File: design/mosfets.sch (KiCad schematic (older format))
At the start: 15 parts, among them Q10 IRFS3006, Q11 IRFS3006, Q12 IRFS3006, Q7 IRFS3006, Q8 IRFS3006, Q9 IRFS3006

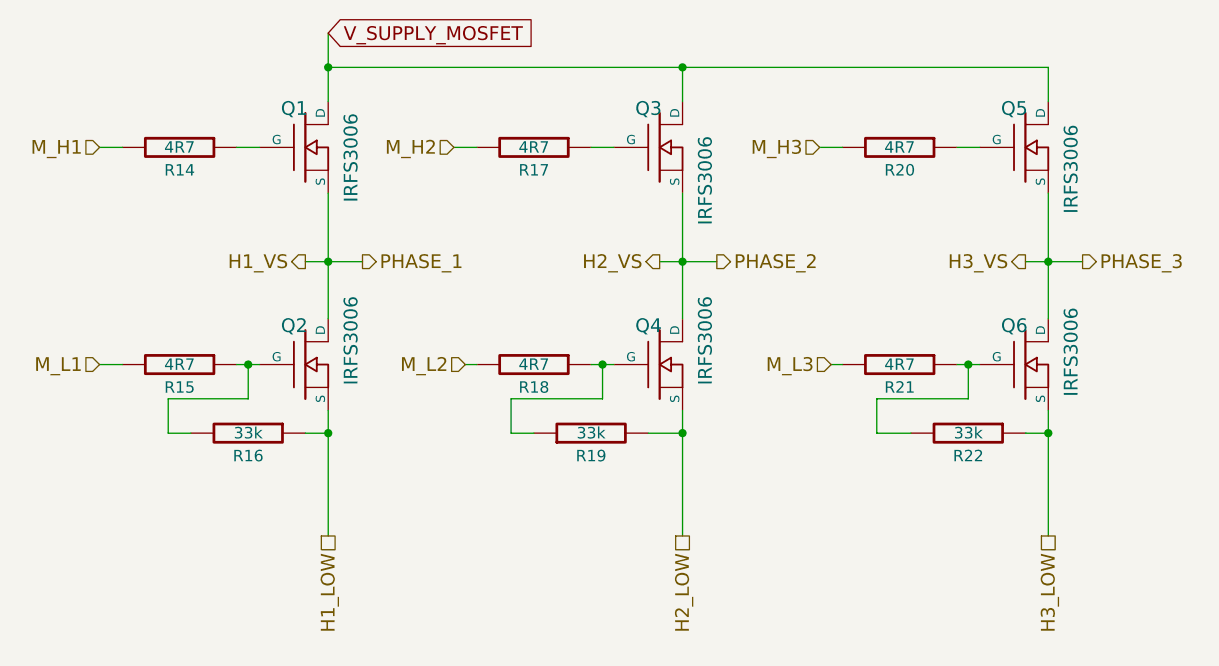
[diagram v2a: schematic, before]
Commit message: Change libraries ot new pretty format
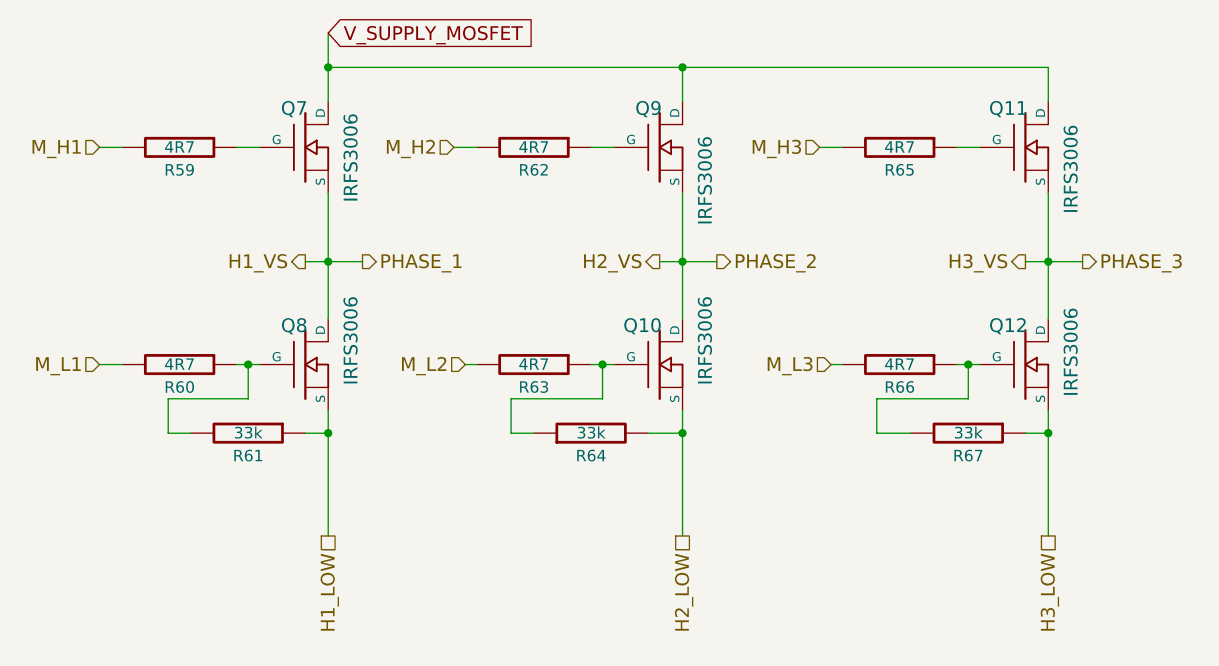
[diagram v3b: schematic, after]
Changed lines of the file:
@@
 AR Path="/54B73596/53F8E60B" Ref="R67"  Part="1"
 AR Path="/53F826DC/53F8E60B" Ref="R22"  Part="1"
-F 0 "R22" V 7950 4050 50  0000 C CNN
+F 0 "R67" V 7950 4050 50  0000 C CNN
 F 1 "33k" V 7850 4050 50  0000 C CNN
 F 2 "SMD_Packages:SMD-0603_r" H 7850 4050 60  0001 C CNN
@@
 AR Path="/54B73596/53F8E612" Ref="R61"  Part="1"
 AR Path="/53F826DC/53F8E612" Ref="R16"  Part="1"
-F 0 "R16" V 4800 4050 50  0000 C CNN
+F 0 "R61" V 4800 4050 50  0000 C CNN
 F 1 "33k" V 4700 4050 50  0000 C CNN
 F 2 "SMD_Packages:SMD-0603_r" H 4700 4050 60  0001 C CNN
@@
 AR Path="/54B73596/53F8E63D" Ref="Q7"  Part="1"
 AR Path="/53F826DC/53F8E63D" Ref="Q1"  Part="1"
-F 0 "Q1" H 4960 2970 60  0000 R CNN
+F 0 "Q7" H 4960 2970 60  0000 R CNN
 F 1 "IRFS3006" V 5150 2950 60  0000 R CNN
 F 2 "CRF1:D2PAK-7-GDS" H 4950 2800 60  0001 C CNN
@@
 AR Path="/54B73596/53F8E644" Ref="Q8"  Part="1"
 AR Path="/53F826DC/53F8E644" Ref="Q2"  Part="1"
-F 0 "Q2" H 4960 3920 60  0000 R CNN
+F 0 "Q8" H 4960 3920 60  0000 R CNN
 F 1 "IRFS3006" V 5150 4050 60  0000 R CNN
 F 2 "CRF1:D2PAK-7-GDS" H 4950 3750 60  0001 C CNN
@@
 AR Path="/54B73596/53F8E64B" Ref="R60"  Part="1"
 AR Path="/53F826DC/53F8E64B" Ref="R15"  Part="1"
-F 0 "R15" V 4500 3750 50  0000 C CNN
+F 0 "R60" V 4500 3750 50  0000 C CNN
 F 1 "4R7" V 4400 3750 50  0000 C CNN
 F 2 "SMD_Packages:SMD-0603_r" H 4400 3750 60  0001 C CNN
@@
 AR Path="/54B73596/53F8E652" Ref="R59"  Part="1"
 AR Path="/53F826DC/53F8E652" Ref="R14"  Part="1"
-F 0 "R14" V 4500 2800 50  0000 C CNN
+F 0 "R59" V 4500 2800 50  0000 C CNN
 F 1 "4R7" V 4400 2800 50  0000 C CNN
 F 2 "SMD_Packages:SMD-0603_r" H 4400 2800 60  0001 C CNN
@@
 AR Path="/54B73596/53F8E65E" Ref="R62"  Part="1"
 AR Path="/53F826DC/53F8E65E" Ref="R17"  Part="1"
-F 0 "R17" V 6050 2800 50  0000 C CNN
+F 0 "R62" V 6050 2800 50  0000 C CNN
 F 1 "4R7" V 5950 2800 50  0000 C CNN
 F 2 "SMD_Packages:SMD-0603_r" H 5950 2800 60  0001 C CNN
@@
 AR Path="/54B73596/53F8E665" Ref="R63"  Part="1"
 AR Path="/53F826DC/53F8E665" Ref="R18"  Part="1"
-F 0 "R18" V 6050 3750 50  0000 C CNN
+F 0 "R63" V 6050 3750 50  0000 C CNN
 F 1 "4R7" V 5950 3750 50  0000 C CNN
 F 2 "SMD_Packages:SMD-0603_r" H 5950 3750 60  0001 C CNN
@@
 AR Path="/54B73596/53F8E66C" Ref="Q10"  Part="1"
 AR Path="/53F826DC/53F8E66C" Ref="Q4"  Part="1"
-F 0 "Q4" H 6510 3920 60  0000 R CNN
+F 0 "Q10" H 6510 3920 60  0000 R CNN
 F 1 "IRFS3006" V 6700 4050 60  0000 R CNN
 F 2 "CRF1:D2PAK-7-GDS" H 6500 3750 60  0001 C CNN
@@
 AR Path="/54B73596/53F8E673" Ref="Q9"  Part="1"
 AR Path="/53F826DC/53F8E673" Ref="Q3"  Part="1"
-F 0 "Q3" H 6510 2970 60  0000 R CNN
+F 0 "Q9" H 6510 2970 60  0000 R CNN
 F 1 "IRFS3006" V 6700 2850 60  0000 R CNN
 F 2 "CRF1:D2PAK-7-GDS" H 6500 2800 60  0001 C CNN
@@
 AR Path="/54B73596/53F8E67A" Ref="Q11"  Part="1"
 AR Path="/53F826DC/53F8E67A" Ref="Q5"  Part="1"
-F 0 "Q5" H 8110 2970 60  0000 R CNN
+F 0 "Q11" H 8110 2970 60  0000 R CNN
 F 1 "IRFS3006" V 8300 2900 60  0000 R CNN
 F 2 "CRF1:D2PAK-7-GDS" H 8100 2800 60  0001 C CNN
@@
 AR Path="/54B73596/53F8E681" Ref="Q12"  Part="1"
 AR Path="/53F826DC/53F8E681" Ref="Q6"  Part="1"
-F 0 "Q6" H 8110 3920 60  0000 R CNN
+F 0 "Q12" H 8110 3920 60  0000 R CNN
 F 1 "IRFS3006" V 8300 4000 60  0000 R CNN
 F 2 "CRF1:D2PAK-7-GDS" H 8100 3750 60  0001 C CNN
@@
 AR Path="/54B73596/53F8E688" Ref="R66"  Part="1"
 AR Path="/53F826DC/53F8E688" Ref="R21"  Part="1"
-F 0 "R21" V 7650 3750 50  0000 C CNN
+F 0 "R66" V 7650 3750 50  0000 C CNN
 F 1 "4R7" V 7550 3750 50  0000 C CNN
 F 2 "SMD_Packages:SMD-0603_r" H 7550 3750 60  0001 C CNN
@@
 AR Path="/54B73596/53F8E68F" Ref="R65"  Part="1"
 AR Path="/53F826DC/53F8E68F" Ref="R20"  Part="1"
-F 0 "R20" V 7650 2800 50  0000 C CNN
+F 0 "R65" V 7650 2800 50  0000 C CNN
 F 1 "4R7" V 7550 2800 50  0000 C CNN
 F 2 "SMD_Packages:SMD-0603_r" H 7550 2800 60  0001 C CNN
@@
 AR Path="/54B73596/53F8E69C" Ref="R64"  Part="1"
 AR Path="/53F826DC/53F8E69C" Ref="R19"  Part="1"
-F 0 "R19" V 6100 4050 50  0000 C CNN
+F 0 "R64" V 6100 4050 50  0000 C CNN
 F 1 "33k" V 6200 4050 50  0000 C CNN
 F 2 "SMD_Packages:SMD-0603_r" H 6200 4050 60  0001 C CNN
@@
 F8 14 F0 0B 42 92 4F 42 07 35 54 00 00 00 00 00 00 7A 11 BC 6D 0C 00 00 00 00 00 F4 2D 50 43 05
 00 00 00 00 00 7D 0B D4 50 01 00 00 00 00 40 DF 02 35 54 00 00 00 00 00 D0 B7 FC 1F 55 28 1C 02
-4B 67 87 83 00 00 00 00 49 45 4E 44 AE 42 60 82 EC $EndBitmap
+4B 67 87 83 00 00 00 00 49 45 4E 44 AE 42 60 82 30 $EndBitmap
 EndData
 $EndBitmap
@@
 00 00 00 41 83 58 05 00 00 08 1A C4 2A 00 00 40 D0 20 56 01 00 00 82 06 B1 0A 00 00 10 34 88 55
 00 00 80 A0 41 AC 02 00 00 04 CD FF 03 15 B2 0E 9E 1D 9F E2 F2 00 00 00 00 49 45 4E 44 AE 42 60
-82 5F $EndBitmap
+82 3F $EndBitmap
 EndData
 $EndBitmap
@@
 6D 12 06 83 C1 60 DA 0B D8 26 61 30 18 0C A6 BD 80 6D 12 06 83 C1 60 DA 0B D8 26 61 30 18 0C A6
 BD 80 6D 12 06 83 C1 60 DA 0B FF 03 68 C2 AC 3A A9 DC 0C E9 00 00 00 00 49 45 4E 44 AE 42 60 82
-23 $EndBitmap
+98 $EndBitmap
 EndData
 $EndBitmap
@@
 40 20 9C 12 44 46 09 04 02 E1 94 20 EE F7 67 02 30 C1 25 10 08 E7 25 24 1A 25 10 08 84 53 82 2C
 11 21 10 08 84 53 82 44 A3 04 02 81 70 4A 10 19 25 10 08 84 53 82 C8 28 81 40 20 9C 12 FF 1F 3E
-01 30 64 8D 18 65 07 00 00 00 00 49 45 4E 44 AE 42 60 82 FD $EndBitmap
+01 30 64 8D 18 65 07 00 00 00 00 49 45 4E 44 AE 42 60 82 0A $EndBitmap
 EndData
 $EndBitmap

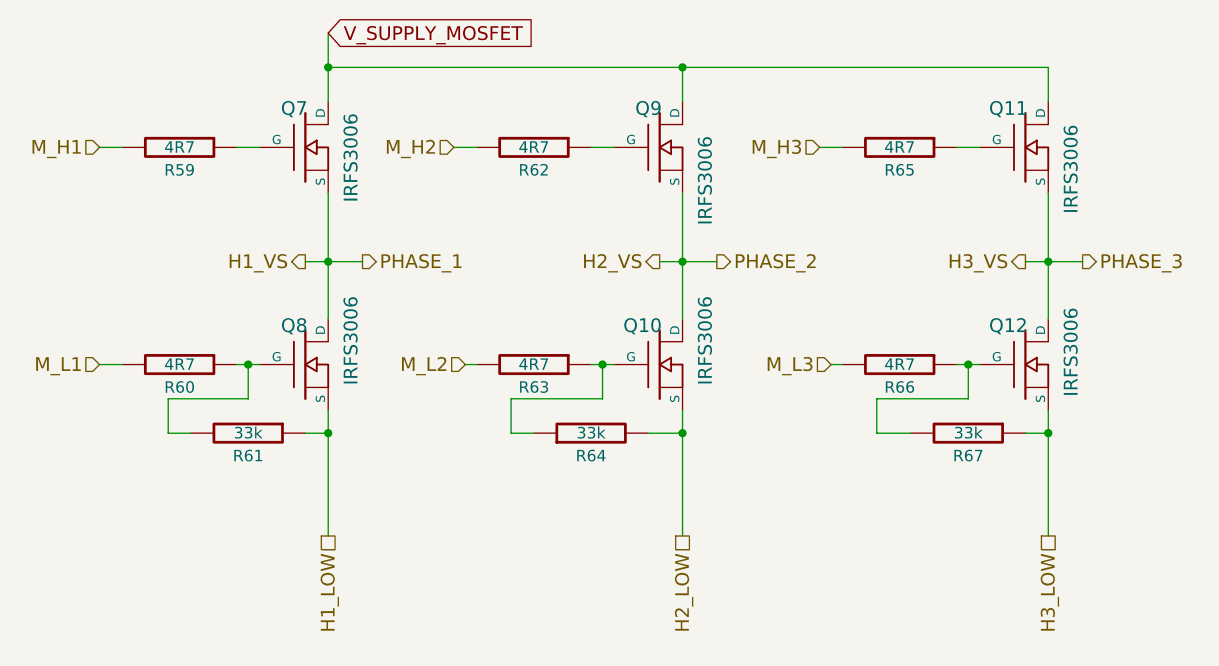
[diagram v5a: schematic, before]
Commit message: Footprint for mosfets and change them in schematics and in netlist
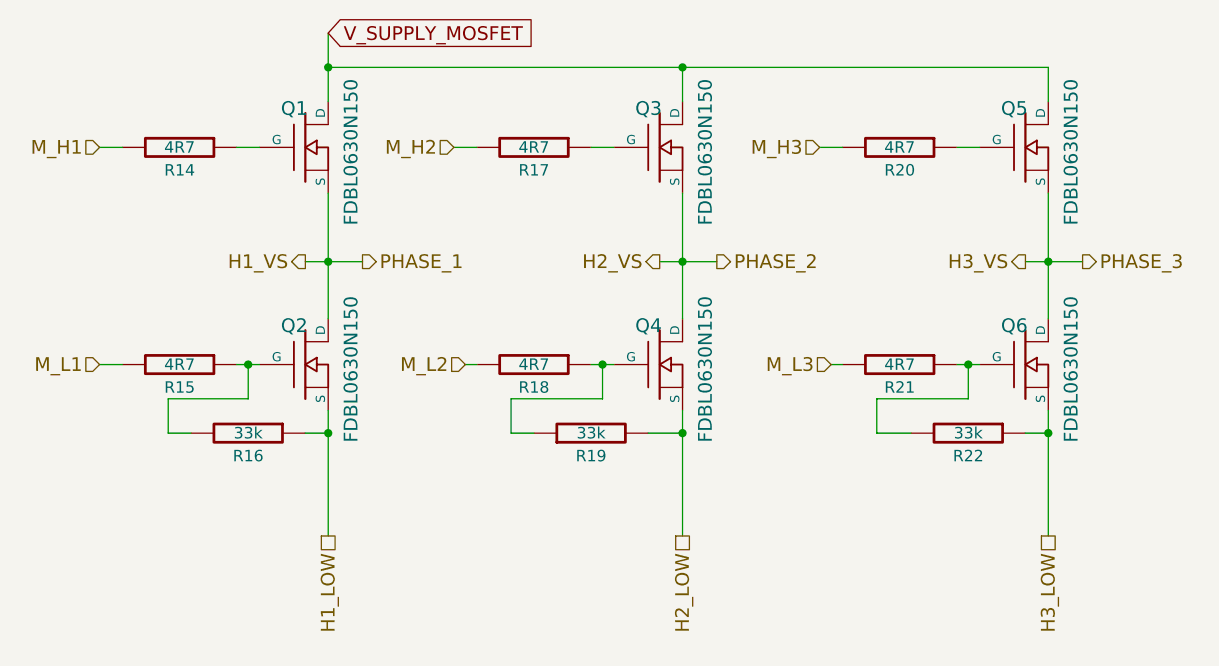
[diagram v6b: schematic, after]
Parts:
- removed Q11, Q12, Q8, Q9: IRFS3006, CRF1:D2PAK-7-GDS, symbol MOSFET_N
- added Q2, Q3, Q5, Q6: FDBL0630N150, H-PSOF:H-PSOF-8L, symbol MOSFET_N
- Q10, Q7: value IRFS3006 -> FDBL0630N150; footprint CRF1:D2PAK-7-GDS -> H-PSOF:H-PSOF-8L
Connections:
- net H1_LOW: now also Q2.S
- net H1_VS: now also Q2.D
- net H2_VS: now also Q3.S
- net H3_LOW: now also Q6.S
- net H3_VS: now also Q5.S, Q6.D
- net V_SUPPLY_MOSFET: now also Q3.D, Q5.D
- net at R66.1, R67.2: now also Q6.G
- net at R60.1, R61.2: now also Q2.G
- net at R62.1: now also Q3.G
- net at R65.1: now also Q5.G
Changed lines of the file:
@@
 AR Path="/54B73596/53F8E60B" Ref="R67"  Part="1"
 AR Path="/53F826DC/53F8E60B" Ref="R22"  Part="1"
-F 0 "R67" V 7950 4050 50  0000 C CNN
+F 0 "R22" V 7950 4050 50  0000 C CNN
 F 1 "33k" V 7850 4050 50  0000 C CNN
 F 2 "SMD_Packages:SMD-0603_r" H 7850 4050 60  0001 C CNN
@@
 AR Path="/54B73596/53F8E612" Ref="R61"  Part="1"
 AR Path="/53F826DC/53F8E612" Ref="R16"  Part="1"
-F 0 "R61" V 4800 4050 50  0000 C CNN
+F 0 "R16" V 4800 4050 50  0000 C CNN
 F 1 "33k" V 4700 4050 50  0000 C CNN
 F 2 "SMD_Packages:SMD-0603_r" H 4700 4050 60  0001 C CNN
@@
 AR Path="/54B73596/53F8E63D" Ref="Q7"  Part="1"
 AR Path="/53F826DC/53F8E63D" Ref="Q1"  Part="1"
-F 0 "Q7" H 4960 2970 60  0000 R CNN
-F 1 "IRFS3006" V 5150 2950 60  0000 R CNN
-F 2 "CRF1:D2PAK-7-GDS" H 4950 2800 60  0001 C CNN
+F 0 "Q1" H 4960 2970 60  0000 R CNN
+F 1 "FDBL0630N150" V 5150 3100 60  0000 R CNN
+F 2 "H-PSOF:H-PSOF-8L" H 4950 2800 60  0001 C CNN
 F 3 "" H 4950 2800 60  0001 C CNN
 	1    4950 2800
-	1    0    0    -1
-$EndComp
-$Comp
-L MOSFET_N Q8
-U 1 1 53F8E644
-P 4950 3750
-AR Path="/54B73596/53F8E644" Ref="Q8"  Part="1"
-AR Path="/53F826DC/53F8E644" Ref="Q2"  Part="1"
-F 0 "Q8" H 4960 3920 60  0000 R CNN
-F 1 "IRFS3006" V 5150 4050 60  0000 R CNN
-F 2 "CRF1:D2PAK-7-GDS" H 4950 3750 60  0001 C CNN
-F 3 "" H 4950 3750 60  0001 C CNN
-	1    4950 3750
 	1    0    0    -1
 $EndComp
@@
 AR Path="/54B73596/53F8E64B" Ref="R60"  Part="1"
 AR Path="/53F826DC/53F8E64B" Ref="R15"  Part="1"
-F 0 "R60" V 4500 3750 50  0000 C CNN
+F 0 "R15" V 4500 3750 50  0000 C CNN
 F 1 "4R7" V 4400 3750 50  0000 C CNN
 F 2 "SMD_Packages:SMD-0603_r" H 4400 3750 60  0001 C CNN
@@
 AR Path="/54B73596/53F8E652" Ref="R59"  Part="1"
 AR Path="/53F826DC/53F8E652" Ref="R14"  Part="1"
-F 0 "R59" V 4500 2800 50  0000 C CNN
+F 0 "R14" V 4500 2800 50  0000 C CNN
 F 1 "4R7" V 4400 2800 50  0000 C CNN
 F 2 "SMD_Packages:SMD-0603_r" H 4400 2800 60  0001 C CNN
@@
 AR Path="/54B73596/53F8E65E" Ref="R62"  Part="1"
 AR Path="/53F826DC/53F8E65E" Ref="R17"  Part="1"
-F 0 "R62" V 6050 2800 50  0000 C CNN
+F 0 "R17" V 6050 2800 50  0000 C CNN
 F 1 "4R7" V 5950 2800 50  0000 C CNN
 F 2 "SMD_Packages:SMD-0603_r" H 5950 2800 60  0001 C CNN
@@
 AR Path="/54B73596/53F8E665" Ref="R63"  Part="1"
 AR Path="/53F826DC/53F8E665" Ref="R18"  Part="1"
-F 0 "R63" V 6050 3750 50  0000 C CNN
+F 0 "R18" V 6050 3750 50  0000 C CNN
 F 1 "4R7" V 5950 3750 50  0000 C CNN
 F 2 "SMD_Packages:SMD-0603_r" H 5950 3750 60  0001 C CNN
@@
 	1    5950 3750
 	0    1    1    0
-$EndComp
-$Comp
-L MOSFET_N Q10
-U 1 1 53F8E66C
-P 6500 3750
-AR Path="/54B73596/53F8E66C" Ref="Q10"  Part="1"
-AR Path="/53F826DC/53F8E66C" Ref="Q4"  Part="1"
-F 0 "Q10" H 6510 3920 60  0000 R CNN
-F 1 "IRFS3006" V 6700 4050 60  0000 R CNN
-F 2 "CRF1:D2PAK-7-GDS" H 6500 3750 60  0001 C CNN
-F 3 "" H 6500 3750 60  0001 C CNN
-	1    6500 3750
-	1    0    0    -1
-$EndComp
-$Comp
-L MOSFET_N Q9
-U 1 1 53F8E673
-P 6500 2800
-AR Path="/54B73596/53F8E673" Ref="Q9"  Part="1"
-AR Path="/53F826DC/53F8E673" Ref="Q3"  Part="1"
-F 0 "Q9" H 6510 2970 60  0000 R CNN
-F 1 "IRFS3006" V 6700 2850 60  0000 R CNN
-F 2 "CRF1:D2PAK-7-GDS" H 6500 2800 60  0001 C CNN
-F 3 "" H 6500 2800 60  0001 C CNN
-	1    6500 2800
-	1    0    0    -1
-$EndComp
-$Comp
-L MOSFET_N Q11
-U 1 1 53F8E67A
-P 8100 2800
-AR Path="/54B73596/53F8E67A" Ref="Q11"  Part="1"
-AR Path="/53F826DC/53F8E67A" Ref="Q5"  Part="1"
-F 0 "Q11" H 8110 2970 60  0000 R CNN
-F 1 "IRFS3006" V 8300 2900 60  0000 R CNN
-F 2 "CRF1:D2PAK-7-GDS" H 8100 2800 60  0001 C CNN
-F 3 "" H 8100 2800 60  0001 C CNN
-	1    8100 2800
-	1    0    0    -1
-$EndComp
-$Comp
-L MOSFET_N Q12
-U 1 1 53F8E681
-P 8100 3750
-AR Path="/54B73596/53F8E681" Ref="Q12"  Part="1"
-AR Path="/53F826DC/53F8E681" Ref="Q6"  Part="1"
-F 0 "Q12" H 8110 3920 60  0000 R CNN
-F 1 "IRFS3006" V 8300 4000 60  0000 R CNN
-F 2 "CRF1:D2PAK-7-GDS" H 8100 3750 60  0001 C CNN
-F 3 "" H 8100 3750 60  0001 C CNN
-	1    8100 3750
-	1    0    0    -1
 $EndComp
 $Comp
@@
 AR Path="/54B73596/53F8E688" Ref="R66"  Part="1"
 AR Path="/53F826DC/53F8E688" Ref="R21"  Part="1"
-F 0 "R66" V 7650 3750 50  0000 C CNN
+F 0 "R21" V 7650 3750 50  0000 C CNN
 F 1 "4R7" V 7550 3750 50  0000 C CNN
 F 2 "SMD_Packages:SMD-0603_r" H 7550 3750 60  0001 C CNN
@@
 AR Path="/54B73596/53F8E68F" Ref="R65"  Part="1"
 AR Path="/53F826DC/53F8E68F" Ref="R20"  Part="1"
-F 0 "R65" V 7650 2800 50  0000 C CNN
+F 0 "R20" V 7650 2800 50  0000 C CNN
 F 1 "4R7" V 7550 2800 50  0000 C CNN
 F 2 "SMD_Packages:SMD-0603_r" H 7550 2800 60  0001 C CNN
@@
 AR Path="/54B73596/53F8E69C" Ref="R64"  Part="1"
 AR Path="/53F826DC/53F8E69C" Ref="R19"  Part="1"
-F 0 "R64" V 6100 4050 50  0000 C CNN
+F 0 "R19" V 6100 4050 50  0000 C CNN
 F 1 "33k" V 6200 4050 50  0000 C CNN
 F 2 "SMD_Packages:SMD-0603_r" H 6200 4050 60  0001 C CNN
@@
 	6450 4050 6600 4050
 Connection ~ 6600 4050
+$Comp
+L MOSFET_N Q2
+U 1 1 54E2030B
+P 4950 3750
+AR Path="/53F826DC/54E2030B" Ref="Q2"  Part="1"
+AR Path="/54B73596/54E2030B" Ref="Q8"  Part="1"
+F 0 "Q2" H 4960 3920 60  0000 R CNN
+F 1 "FDBL0630N150" V 5150 4050 60  0000 R CNN
+F 2 "H-PSOF:H-PSOF-8L" H 4950 3750 60  0001 C CNN
+F 3 "" H 4950 3750 60  0001 C CNN
+	1    4950 3750
+	1    0    0    -1
+$EndComp
+$Comp
+L MOSFET_N Q3
+U 1 1 54E2035A
+P 6500 2800
+AR Path="/53F826DC/54E2035A" Ref="Q3"  Part="1"
+AR Path="/54B73596/54E2035A" Ref="Q9"  Part="1"
+F 0 "Q3" H 6510 2970 60  0000 R CNN
+F 1 "FDBL0630N150" V 6700 3100 60  0000 R CNN
+F 2 "H-PSOF:H-PSOF-8L" H 6500 2800 60  0001 C CNN
+F 3 "" H 6500 2800 60  0001 C CNN
+	1    6500 2800
+	1    0    0    -1
+$EndComp
+$Comp
+L MOSFET_N Q5
+U 1 1 54E20388
+P 8100 2800
+AR Path="/53F826DC/54E20388" Ref="Q5"  Part="1"
+AR Path="/54B73596/54E20388" Ref="Q11"  Part="1"
+F 0 "Q5" H 8110 2970 60  0000 R CNN
+F 1 "FDBL0630N150" V 8300 3100 60  0000 R CNN
+F 2 "H-PSOF:H-PSOF-8L" H 8100 2800 60  0001 C CNN
+F 3 "" H 8100 2800 60  0001 C CNN
+	1    8100 2800
+	1    0    0    -1
+$EndComp
+$Comp
+L MOSFET_N Q6
+U 1 1 54E203B7
+P 8100 3750
+AR Path="/53F826DC/54E203B7" Ref="Q6"  Part="1"
+AR Path="/54B73596/54E203B7" Ref="Q12"  Part="1"
+F 0 "Q6" H 8110 3920 60  0000 R CNN
+F 1 "FDBL0630N150" V 8300 4050 60  0000 R CNN
+F 2 "H-PSOF:H-PSOF-8L" H 8100 3750 60  0001 C CNN
+F 3 "" H 8100 3750 60  0001 C CNN
+	1    8100 3750
+	1    0    0    -1
+$EndComp
+$Comp
+L MOSFET_N Q10
+U 1 1 54E20407
+P 6500 3750
+AR Path="/54B73596/54E20407" Ref="Q10"  Part="1"
+AR Path="/53F826DC/54E20407" Ref="Q4"  Part="1"
+F 0 "Q4" H 6510 3920 60  0000 R CNN
+F 1 "FDBL0630N150" V 6700 4050 60  0000 R CNN
+F 2 "H-PSOF:H-PSOF-8L" H 6500 3750 60  0001 C CNN
+F 3 "" H 6500 3750 60  0001 C CNN
+	1    6500 3750
+	1    0    0    -1
+$EndComp
 $EndSCHEMATC
